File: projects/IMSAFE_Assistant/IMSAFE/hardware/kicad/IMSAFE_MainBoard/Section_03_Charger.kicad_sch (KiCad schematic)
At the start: 0 parts

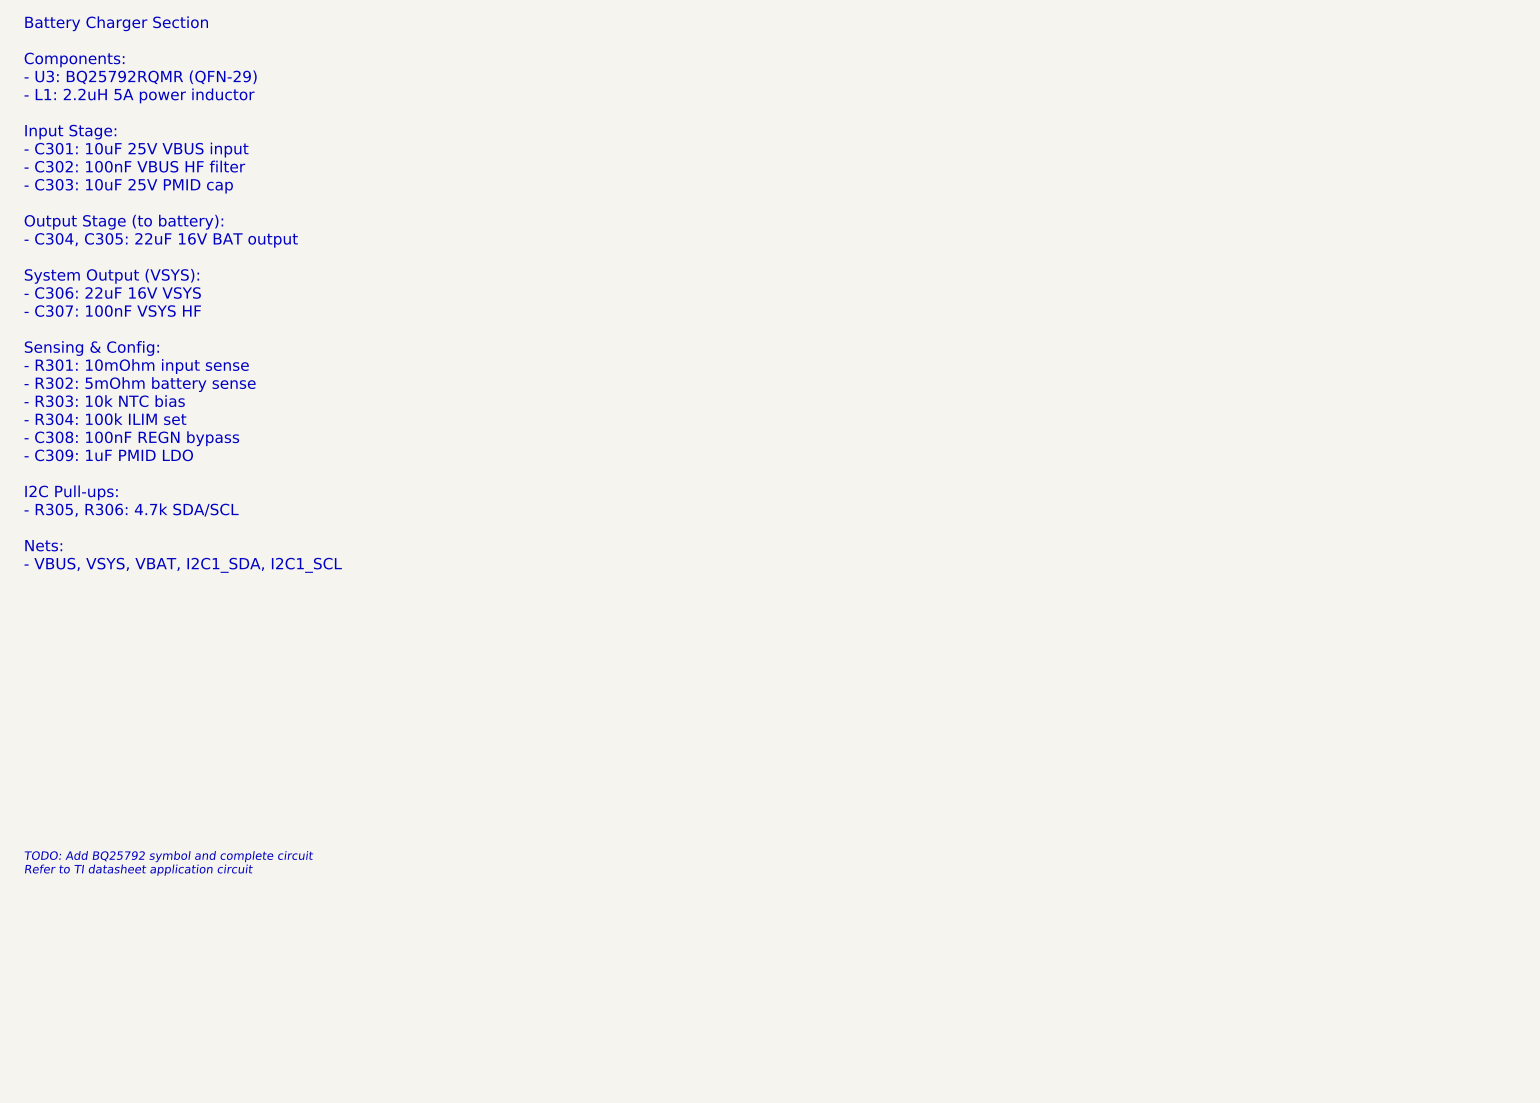
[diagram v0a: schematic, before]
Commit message: Add schematic circuits for MCU, USB-C, and Charger sections
Section 01 (MCU Core):
- STM32H747 decoupling network (22 caps per AN4661)
- HSE 8MHz and LSE 32.768kHz crystal circuits
- Reset circuit with pull-up and filter
- BOOT0 pull-down for flash boot

Section 02 (USB-C Input):
- USB-C 16-pin receptacle with CC resistors (UFP sink)
- USBLC6-2SC6 ESD protection on D+/D-
- VBUS filtering (100nF + 10uF)

Section 03 (Battery Charger):
- BQ25792 buck-boost charger with NVDC power-path
- 2.2uH power inductor
- Input, output, and system capacitors
- Current sense resistors and I2C pull-ups

Co-Authored-By: Claude Opus 4.5 <noreply@anthropic.com>
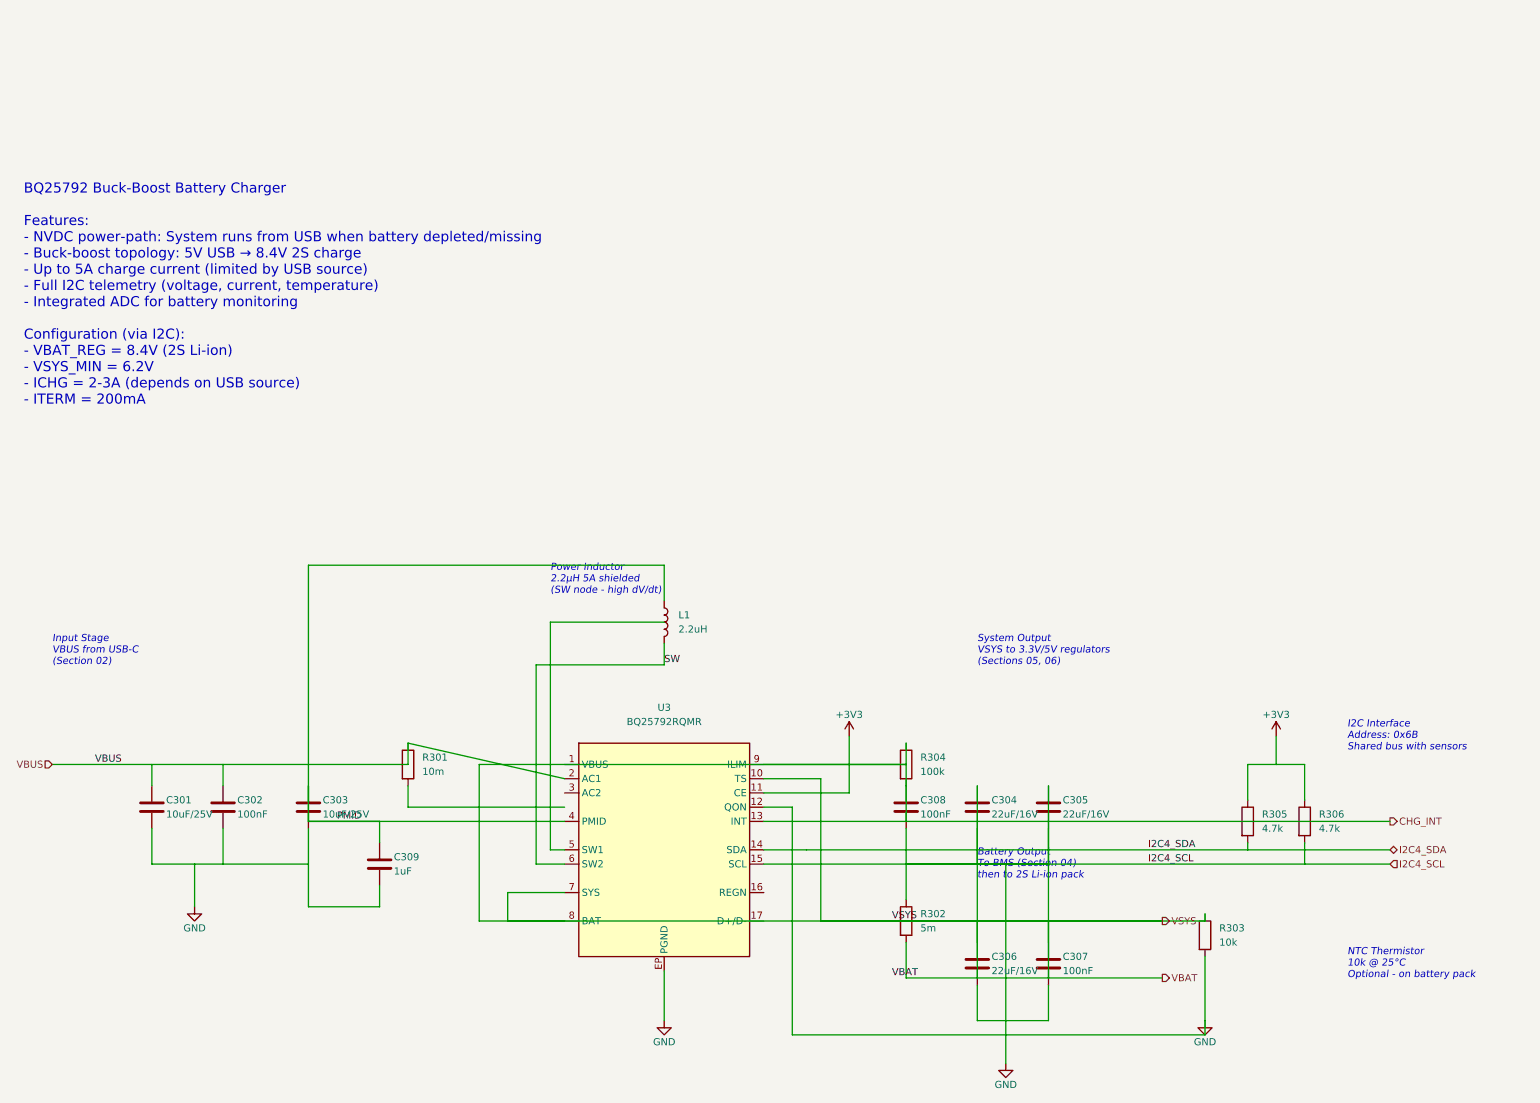
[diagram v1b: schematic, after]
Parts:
- added C301, C303: 10uF/25V, Capacitor_SMD:C_0805_2012Metric, symbol Device:C
- added C302, C307, C308: 100nF, Capacitor_SMD:C_0603_1608Metric, symbol Device:C
- added C304, C305, C306: 22uF/16V, Capacitor_SMD:C_0805_2012Metric, symbol Device:C
- added C309: 1uF, Capacitor_SMD:C_0603_1608Metric, symbol Device:C
- added L1: 2.2uH, Inductor_SMD:L_Bourns_SRN5040, symbol Device:L
- added R301: 10m, Resistor_SMD:R_0805_2012Metric, symbol Device:R
- added R302: 5m, Resistor_SMD:R_1206_3216Metric, symbol Device:R
- added R303: 10k, Resistor_SMD:R_0603_1608Metric, symbol Device:R
- added R304: 100k, Resistor_SMD:R_0603_1608Metric, symbol Device:R
- added R305, R306: 4.7k, Resistor_SMD:R_0603_1608Metric, symbol Device:R
- added U3: BQ25792RQMR, Package_DFN_QFN:QFN-29-1EP_4x4mm_P0.4mm_EP2.65x2.65mm, symbol BQ25792:BQ25792
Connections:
- new net +3V3: R305.1, R306.1, U3.11 (CE)
- new net CHG_INT: U3.13 (INT)
- new net GND: C301.2, C302.2, C303.2, C304.1, C304.2, C305.1, C305.2, C306.1, C306.2, C307.1, C307.2, C308.1, C308.2, C309.2, R302.1, R302.2, R303.1, R303.2, R304.1, R304.2, R306.2, U3.10 (TS), U3.12 (QON), U3.15 (SCL), U3.7 (SYS), U3.8 (BAT), U3.9 (ILIM), U3.EP (PGND)
- new net I2C4_SDA: R305.2, U3.14 (SDA)
- new net PMID: C303.1, C309.1, L1.1, U3.4 (PMID)
- new net SW: L1.2, U3.6 (SW2)
- new net VBUS: C301.1, C302.1, R301.1, U3.2 (AC1)
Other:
- note added: "BQ25792 Buck-Boost Battery Charger Features: - NVDC power-path: System runs from USB when battery depleted/missing - Buck-boost topology: 5V USB → 8.4V 2S charge - Up to 5A charge current (limited by USB source) - Full I2C telemetry (voltage, current, temperature) - Integrated ADC for battery monitoring Configuration (via I2C): - VBAT_REG = 8.4V (2S Li-ion) - VSYS_MIN = 6.2V - ICHG = 2-3A (depend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"
- note added: "Battery Output To BMS (Section 04) then to 2S Li-ion pack"
- note added: "I2C Interface Address: 0x6B Shared bus with sensors"
- note added: "Input Stage VBUS from USB-C (Section 02)"
- note added: "NTC Thermistor 10k @ 25°C Optional - on battery pack"
- note added: "Power Inductor 2.2µH 5A shielded (SW node - high dV/dt)"
- note added: "System Output VSYS to 3.3V/5V regulators (Sections 05, 06)"
- note removed: "Battery Charger Section Components: - U3: BQ25792RQMR (QFN-29) - L1: 2.2uH 5A power inductor Input Stage: - C301: 10uF 25V VBUS input - C302: 100nF VBUS HF filter - C303: 10uF 25V PMID cap Output Stage (to battery): - C304, C305: 22uF 16V BAT output System Output (VSYS): - C306: 22uF 16V VSYS - C307: 100nF VSYS HF Sensing & Config: - R301: 10mOhm input sense - R302: 5mOhm battery sense - R303: 10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"
- note removed: "TODO: Add BQ25792 symbol and complete circuit Refer to TI datasheet application circuit"

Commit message: Update KiCad schematics and add analysis files
- Update all MainBoard schematic sections with component placement
- Add ERC reports and analysis scripts for schematic validation
- Update Radar Interface and SwitchLED Board projects
- Sync KiCad project files with latest session changes

Co-Authored-By: Claude Opus 4.5 <noreply@anthropic.com>
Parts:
- removed C301, C303: 10uF/25V, Capacitor_SMD:C_0805_2012Metric, symbol Device:C
- removed C302, C307, C308: 100nF, Capacitor_SMD:C_0603_1608Metric, symbol Device:C
- removed C304, C305, C306: 22uF/16V, Capacitor_SMD:C_0805_2012Metric, symbol Device:C
- removed C309: 1uF, Capacitor_SMD:C_0603_1608Metric, symbol Device:C
- removed R301: 10m, Resistor_SMD:R_0805_2012Metric, symbol Device:R
- removed R302: 5m, Resistor_SMD:R_1206_3216Metric, symbol Device:R
- removed R303: 10k, Resistor_SMD:R_0603_1608Metric, symbol Device:R
- removed R304: 100k, Resistor_SMD:R_0603_1608Metric, symbol Device:R
- removed R305, R306: 4.7k, Resistor_SMD:R_0603_1608Metric, symbol Device:R
- removed U3: BQ25792RQMR, Package_DFN_QFN:QFN-29-1EP_4x4mm_P0.4mm_EP2.65x2.65mm, symbol BQ25792:BQ25792
- added BT1, BT2: Battery_Cell, symbol Device:Battery_Cell
- added C1, C13, C14, C15, C3, C4, C5, C6, C7, C9: 10uF/25V, Capacitor_SMD:C_0805_2012Metric, symbol Device:C
- added C10, C12: 47nF, Capacitor_SMD:C_0603_1608Metric, symbol Device:C
- added C11: 4.7uF, Capacitor_SMD:C_0603_1608Metric, symbol Device:C
- added C16: 1 nF, Capacitor_SMD:C_0805_2012Metric, symbol Device:C
- added C17, C19, C20: 10uF, Capacitor_SMD:C_0805_2012Metric, symbol Device:C
- added C18, C2, C8: 100nF, Capacitor_SMD:C_0603_1608Metric, symbol Device:C
- added J1: Conn_01x05_Pin, symbol Connector:Conn_01x05_Pin
- added J2: Conn_01x05_Socket, symbol Connector:Conn_01x05_Socket
- added R1, R?: 4.7k, Resistor_SMD:R_0603_1608Metric, symbol Device:R
- added R2: 100, Resistor_SMD:R_0603_1608Metric, symbol Device:R
- added TH1: Thermistor_NTC, symbol Device:Thermistor_NTC
- added U1: BQ25792RQMR, RQM0029A-MFG, symbol 1_New_library:BQ25792RQMR
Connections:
- net +3V3: now also R1.1, R?.1
- net CHG_INT: now also U1.21 (INT_N)
- net GND: now also C1.2, C11.2, C14.2, C15.2, C16.2, C17.2, C18.2, C19.2, C2.2, C20.2, C3.2, C4.2, C5.2, C6.2, C7.2, C8.2, C9.2, J1.1 (Pin_1), J1.3 (Pin_3), U1.10 (ACDRV2), U1.11 (ACDRV1), U1.27 (GND)
- net I2C4_SDA: now also R?.2, U1.15 (SDA)
- net VBUS: now also C7.1, C8.1, C9.1, U1.2 (VBUS), U1.3 (VBUS), U1.8 (VAC2), U1.9 (VAC1)
- net PMID: no longer names the net of L1.1
- net PMID: now also C10.2, U1.28 (SW1)
- net SW: no longer names the net of L1.2
- net SW: now also C12.2, U1.26 (SW2)
- new net: J2.2 (Pin_2), TH1.1
- new net: J2.1 (Pin_1), TH1.2
- new net: BT1.1 (+), J2.5 (Pin_5)
- new net: BT1.2 (-), BT2.1 (+)
- new net: C11.1, J1.2 (Pin_2), U1.16 (TS), U1.17 (ILIM_HIZ), U1.5 (REGN)
- new net: R2.1, U1.18 (BATP)
- new net: C12.1, U1.19 (BTST2)
- new net: C14.1, C15.1, J1.5 (Pin_5), R2.2, U1.22 (BAT), U1.23 (BAT)
- new net: C16.1, U1.24 (SDRV)
- new net: C17.1, C18.1, C19.1, C20.1, U1.29 (PMID)
- new net: C10.1, U1.4 (BTST1)
- new net: BT2.2 (-), J2.3 (Pin_3)
- new net I2C4_SCL: R1.2, U1.14 (SCL)
- new net VSYS: C1.1, C2.1, C3.1, C4.1, C5.1, C6.1, U1.25 (SYS)
